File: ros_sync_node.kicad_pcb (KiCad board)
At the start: 2 copper layers, 42.5 x 38.5 mm, 16 parts, among them J1 Conn_01x03_Male, J10 5V_In, J11 3V3_Out, J2 Conn_01x03_Male, J3 Conn_01x03_Male, J4 Conn_01x03_Male, J5 Conn_01x03_Male, J6 Conn_01x03_Male, J7 Conn_01x03_Male, J8 Conn_01x03_Male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

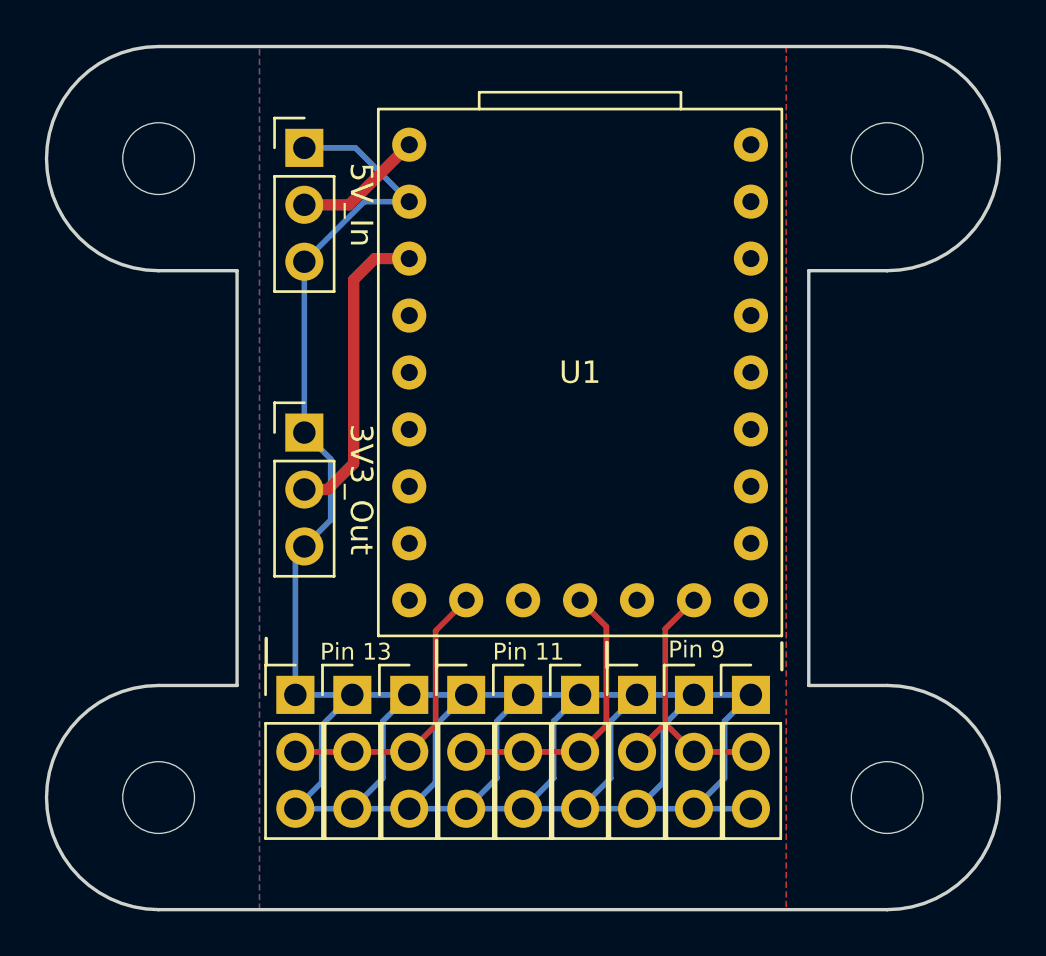
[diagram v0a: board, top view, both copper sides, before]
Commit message: Added mousebites and a readme
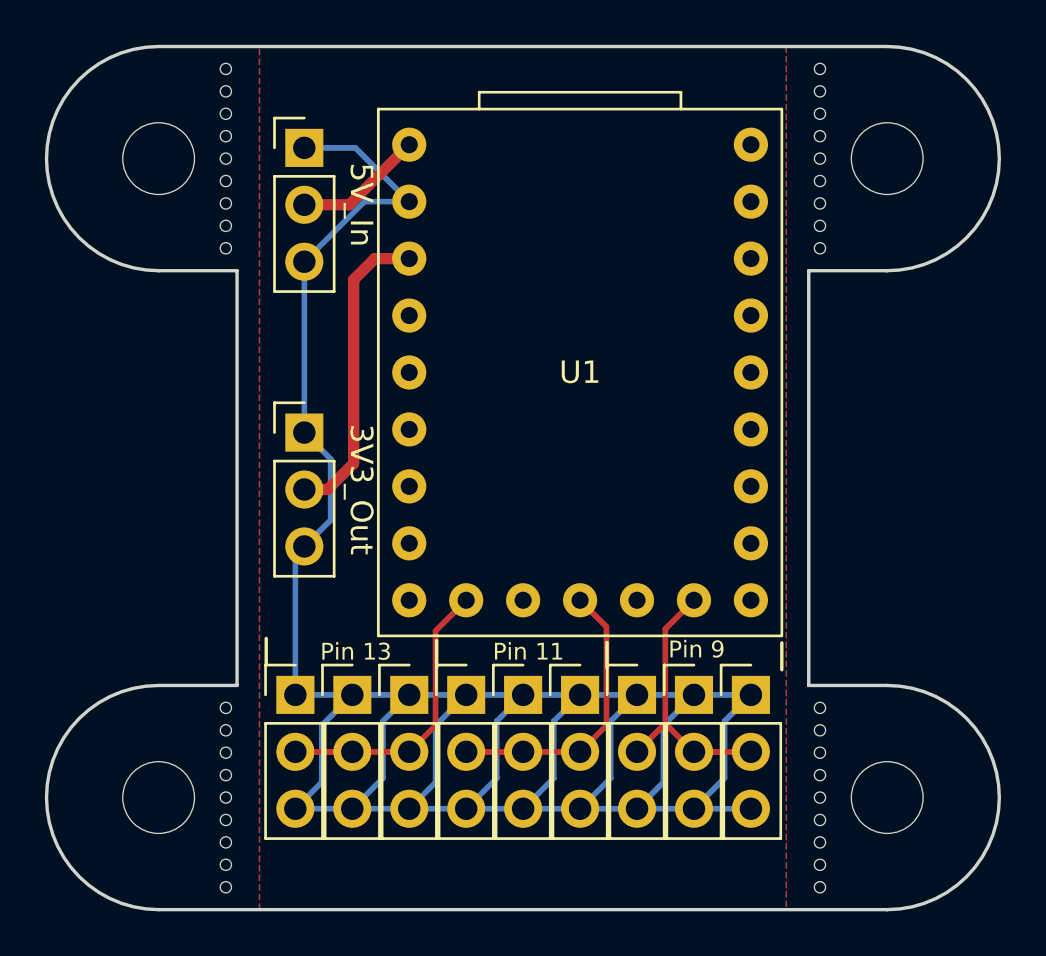
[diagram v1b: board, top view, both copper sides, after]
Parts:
- added H10: MountingHole, other:OSHTab, F.Cu at (176.0, 99.5)
- added H11: MountingHole, other:OSHTab, F.Cu at (176.0, 68.0)
- added H12: MountingHole, other:OSHTab, F.Cu at (176.0, 102.5)
- added H13: MountingHole, other:OSHTab, F.Cu at (176.0, 71.0)
- added H14: MountingHole, other:OSHTab, F.Cu at (149.5, 102.5)
- added H15: MountingHole, other:OSHTab, F.Cu at (149.5, 99.5)
- added H16: MountingHole, other:OSHTab, F.Cu at (176.0, 74.0)
- added H5: MountingHole, other:OSHTab, F.Cu at (149.5, 74.0)
- added H6: MountingHole, other:OSHTab, F.Cu at (149.5, 96.5)
- added H7: MountingHole, other:OSHTab, F.Cu at (149.5, 71.0)
- added H8: MountingHole, other:OSHTab, F.Cu at (149.5, 68.0)
- added H9: MountingHole, other:OSHTab, F.Cu at (176.0, 96.5)
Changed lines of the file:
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@@
     (tracks 57)
     (zones 0)
-    (modules 16)
+    (modules 28)
     (nets 24)
   )
@@
     (add_net +5V)
   )
+  (module other:OSHTab (layer F.Cu)
+    (at 176 74 270)
+    (descr "0.5mm holes and 3mm wide tab")
+    (tags "OSHPark recommended panel tab")
+    (attr virtual)
+    (fp_text reference H16 (at 0 -1.25 90) (layer F.Fab) hide
+      (effects (font (size 1 1) (thickness 0.15)))
+    )
+    (fp_text value MountingHole (at 0 1.25 90) (layer F.Fab)
+      (effects (font (size 1 1) (thickness 0.15)))
+    )
+    (pad "" np_thru_hole circle (at 1 0 270) (size 0.5 0.5) (drill 0.5) (layers *.Cu))
+    (pad "" np_thru_hole circle (at -1 0 270) (size 0.5 0.5) (drill 0.5) (layers *.Cu))
+    (pad "" np_thru_hole circle (at 0 0 270) (size 0.5 0.5) (drill 0.5) (layers *.Cu))
+  )
+  (module other:OSHTab (layer F.Cu)
+    (at 149.5 99.5 90)
+    (descr "0.5mm holes and 3mm wide tab")
+    (tags "OSHPark recommended panel tab")
+    (attr virtual)
+    (fp_text reference H15 (at 0 -1.25 90) (layer F.Fab) hide
+      (effects (font (size 1 1) (thickness 0.15)))
+    )
+    (fp_text value MountingHole (at 0 1.25 90) (layer F.Fab)
+      (effects (font (size 1 1) (thickness 0.15)))
+    )
+    (pad "" np_thru_hole circle (at 1 0 90) (size 0.5 0.5) (drill 0.5) (layers *.Cu))
+    (pad "" np_thru_hole circle (at -1 0 90) (size 0.5 0.5) (drill 0.5) (layers *.Cu))
+    (pad "" np_thru_hole circle (at 0 0 90) (size 0.5 0.5) (drill 0.5) (layers *.Cu))
+  )
+  (module other:OSHTab (layer F.Cu)
+    (at 149.5 102.5 90)
+    (descr "0.5mm holes and 3mm wide tab")
+    (tags "OSHPark recommended panel tab")
+    (attr virtual)
+    (fp_text reference H14 (at 0 -1.25 90) (layer F.Fab) hide
+      (effects (font (size 1 1) (thickness 0.15)))
+    )
+    (fp_text value MountingHole (at 0 1.25 90) (layer F.Fab)
+      (effects (font (size 1 1) (thickness 0.15)))
+    )
+    (pad "" np_thru_hole circle (at 1 0 90) (size 0.5 0.5) (drill 0.5) (layers *.Cu))
+    (pad "" np_thru_hole circle (at -1 0 90) (size 0.5 0.5) (drill 0.5) (layers *.Cu))
+    (pad "" np_thru_hole circle (at 0 0 90) (size 0.5 0.5) (drill 0.5) (layers *.Cu))
+  )
+  (module other:OSHTab (layer F.Cu)
+    (at 176 71 270)
+    (descr "0.5mm holes and 3mm wide tab")
+    (tags "OSHPark recommended panel tab")
+    (attr virtual)
+    (fp_text reference H13 (at 0 -1.25 90) (layer F.Fab) hide
+      (effects (font (size 1 1) (thickness 0.15)))
+    )
+    (fp_text value MountingHole (at 0 1.25 90) (layer F.Fab)
+      (effects (font (size 1 1) (thickness 0.15)))
+    )
+    (pad "" np_thru_hole circle (at 1 0 270) (size 0.5 0.5) (drill 0.5) (layers *.Cu))
+    (pad "" np_thru_hole circle (at -1 0 270) (size 0.5 0.5) (drill 0.5) (layers *.Cu))
+    (pad "" np_thru_hole circle (at 0 0 270) (size 0.5 0.5) (drill 0.5) (layers *.Cu))
+  )
+  (module other:OSHTab (layer F.Cu)
+    (at 176 102.5 270)
+    (descr "0.5mm holes and 3mm wide tab")
+    (tags "OSHPark recommended panel tab")
+    (attr virtual)
+    (fp_text reference H12 (at 0 -1.25 90) (layer F.Fab) hide
+      (effects (font (size 1 1) (thickness 0.15)))
+    )
+    (fp_text value MountingHole (at 0 1.25 90) (layer F.Fab)
+      (effects (font (size 1 1) (thickness 0.15)))
+    )
+    (pad "" np_thru_hole circle (at 1 0 270) (size 0.5 0.5) (drill 0.5) (layers *.Cu))
+    (pad "" np_thru_hole circle (at -1 0 270) (size 0.5 0.5) (drill 0.5) (layers *.Cu))
+    (pad "" np_thru_hole circle (at 0 0 270) (size 0.5 0.5) (drill 0.5) (layers *.Cu))
+  )
+  (module other:OSHTab (layer F.Cu)
+    (at 176 68 270)
+    (descr "0.5mm holes and 3mm wide tab")
+    (tags "OSHPark recommended panel tab")
+    (attr virtual)
+    (fp_text reference H11 (at 0 -1.25 90) (layer F.Fab) hide
+      (effects (font (size 1 1) (thickness 0.15)))
+    )
+    (fp_text value MountingHole (at 0 1.25 90) (layer F.Fab)
+      (effects (font (size 1 1) (thickness 0.15)))
+    )
+    (pad "" np_thru_hole circle (at 1 0 270) (size 0.5 0.5) (drill 0.5) (layers *.Cu))
+    (pad "" np_thru_hole circle (at -1 0 270) (size 0.5 0.5) (drill 0.5) (layers *.Cu))
+    (pad "" np_thru_hole circle (at 0 0 270) (size 0.5 0.5) (drill 0.5) (layers *.Cu))
+  )
+  (module other:OSHTab (layer F.Cu)
+    (at 176 99.5 270)
+    (descr "0.5mm holes and 3mm wide tab")
+    (tags "OSHPark recommended panel tab")
+    (attr virtual)
+    (fp_text reference H10 (at 0 -1.25 90) (layer F.Fab) hide
+      (effects (font (size 1 1) (thickness 0.15)))
+    )
+    (fp_text value MountingHole (at 0 1.25 90) (layer F.Fab)
+      (effects (font (size 1 1) (thickness 0.15)))
+    )
+    (pad "" np_thru_hole circle (at 1 0 270) (size 0.5 0.5) (drill 0.5) (layers *.Cu))
+    (pad "" np_thru_hole circle (at -1 0 270) (size 0.5 0.5) (drill 0.5) (layers *.Cu))
+    (pad "" np_thru_hole circle (at 0 0 270) (size 0.5 0.5) (drill 0.5) (layers *.Cu))
+  )
+  (module other:OSHTab (layer F.Cu)
+    (at 176 96.5 270)
+    (descr "0.5mm holes and 3mm wide tab")
+    (tags "OSHPark recommended panel tab")
+    (attr virtual)
+    (fp_text reference H9 (at 0 -1.25 90) (layer F.Fab) hide
+      (effects (font (size 1 1) (thickness 0.15)))
+    )
+    (fp_text value MountingHole (at 0 1.25 90) (layer F.Fab)
+      (effects (font (size 1 1) (thickness 0.15)))
+    )
+    (pad "" np_thru_hole circle (at 1 0 270) (size 0.5 0.5) (drill 0.5) (layers *.Cu))
+    (pad "" np_thru_hole circle (at -1 0 270) (size 0.5 0.5) (drill 0.5) (layers *.Cu))
+    (pad "" np_thru_hole circle (at 0 0 270) (size 0.5 0.5) (drill 0.5) (layers *.Cu))
+  )
+  (module other:OSHTab (layer F.Cu)
+    (at 149.5 68 90)
+    (descr "0.5mm holes and 3mm wide tab")
+    (tags "OSHPark recommended panel tab")
+    (attr virtual)
+    (fp_text reference H8 (at 0 -1.25 90) (layer F.Fab) hide
+      (effects (font (size 1 1) (thickness 0.15)))
+    )
+    (fp_text value MountingHole (at 0 1.25 90) (layer F.Fab)
+      (effects (font (size 1 1) (thickness 0.15)))
+    )
+    (pad "" np_thru_hole circle (at 1 0 90) (size 0.5 0.5) (drill 0.5) (layers *.Cu))
+    (pad "" np_thru_hole circle (at -1 0 90) (size 0.5 0.5) (drill 0.5) (layers *.Cu))
+    (pad "" np_thru_hole circle (at 0 0 90) (size 0.5 0.5) (drill 0.5) (layers *.Cu))
+  )
+  (module other:OSHTab (layer F.Cu)
+    (at 149.5 71 90)
+    (descr "0.5mm holes and 3mm wide tab")
+    (tags "OSHPark recommended panel tab")
+    (attr virtual)
+    (fp_text reference H7 (at 0 -1.25 90) (layer F.Fab) hide
+      (effects (font (size 1 1) (thickness 0.15)))
+    )
+    (fp_text value MountingHole (at 0 1.25 90) (layer F.Fab)
+      (effects (font (size 1 1) (thickness 0.15)))
+    )
+    (pad "" np_thru_hole circle (at 1 0 90) (size 0.5 0.5) (drill 0.5) (layers *.Cu))
+    (pad "" np_thru_hole circle (at -1 0 90) (size 0.5 0.5) (drill 0.5) (layers *.Cu))
+    (pad "" np_thru_hole circle (at 0 0 90) (size 0.5 0.5) (drill 0.5) (layers *.Cu))
+  )
+  (module other:OSHTab (layer F.Cu)
+    (at 149.5 96.5 90)
+    (descr "0.5mm holes and 3mm wide tab")
+    (tags "OSHPark recommended panel tab")
+    (attr virtual)
+    (fp_text reference H6 (at 0 -1.25 90) (layer F.Fab) hide
+      (effects (font (size 1 1) (thickness 0.15)))
+    )
+    (fp_text value MountingHole (at 0 1.25 90) (layer F.Fab)
+      (effects (font (size 1 1) (thickness 0.15)))
+    )
+    (pad "" np_thru_hole circle (at 1 0 90) (size 0.5 0.5) (drill 0.5) (layers *.Cu))
+    (pad "" np_thru_hole circle (at -1 0 90) (size 0.5 0.5) (drill 0.5) (layers *.Cu))
+    (pad "" np_thru_hole circle (at 0 0 90) (size 0.5 0.5) (drill 0.5) (layers *.Cu))
+  )
+  (module other:OSHTab (layer F.Cu)
+    (at 149.5 74 90)
+    (descr "0.5mm holes and 3mm wide tab")
+    (tags "OSHPark recommended panel tab")
+    (attr virtual)
+    (fp_text reference H5 (at 0 -1.25 90) (layer F.Fab) hide
+      (effects (font (size 1 1) (thickness 0.15)))
+    )
+    (fp_text value MountingHole (at 0 1.25 90) (layer F.Fab)
+      (effects (font (size 1 1) (thickness 0.15)))
+    )
+    (pad "" np_thru_hole circle (at 1 0 90) (size 0.5 0.5) (drill 0.5) (layers *.Cu))
+    (pad "" np_thru_hole circle (at -1 0 90) (size 0.5 0.5) (drill 0.5) (layers *.Cu))
+    (pad "" np_thru_hole circle (at 0 0 90) (size 0.5 0.5) (drill 0.5) (layers *.Cu))
+  )
   (module MountingHole:MountingHole_3.2mm_M3 (layer F.Cu)

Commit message: Added output pin for the neopixels.  Update to KiCAD 7
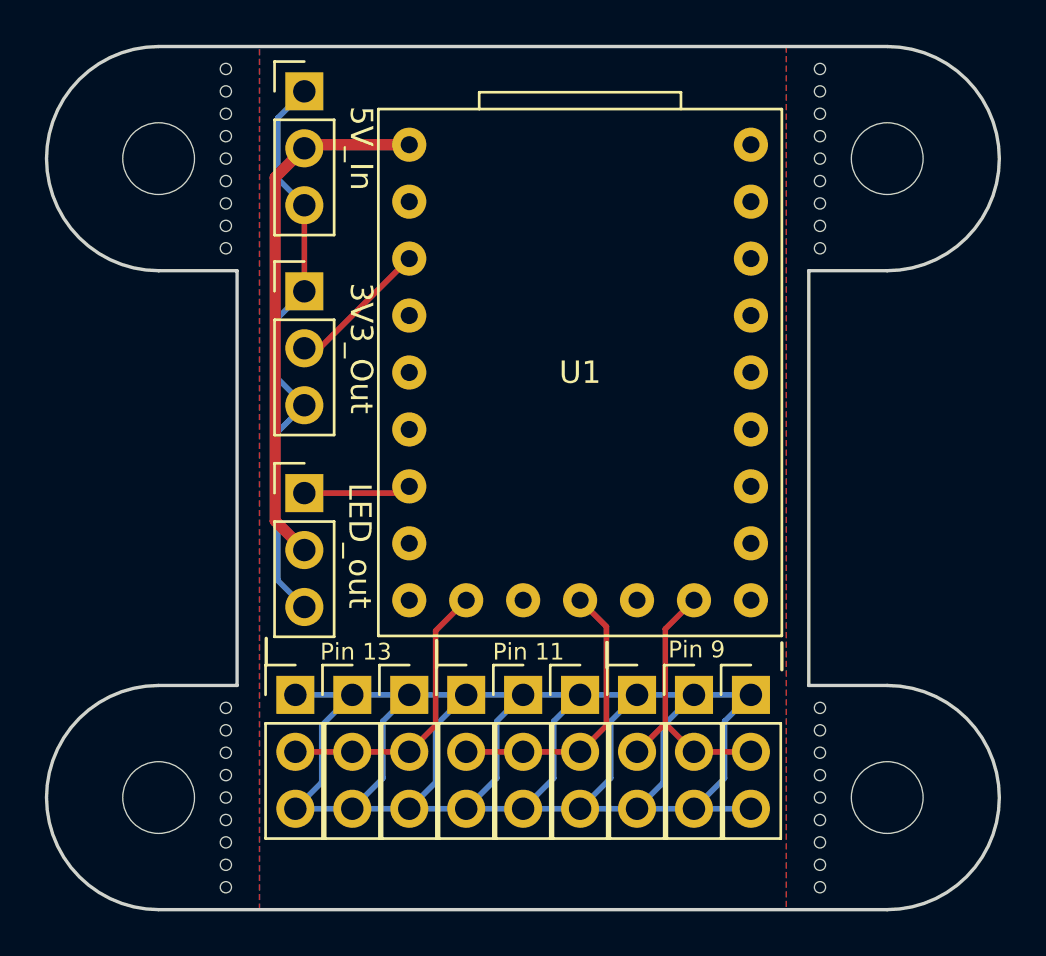
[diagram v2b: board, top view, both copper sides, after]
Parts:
- added J12: LED_out, Connector_PinHeader_2.54mm:PinHeader_1x03_P2.54mm_Vertical, F.Cu at (153.0, 85.9)
- J1, J2, J3, J4, J5, J6, J7, J8, J9: value Conn_01x03_Male -> Conn_01x03_Pin
- moved J11 6.30 mm to (153.0, 76.9)
- moved J10 2.52 mm to (153.0, 68.0)
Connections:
- net +3V3 renamed +3.3V
- U1 pad 0: Net-(U1-Pad0) -> unconnected-(U1-Pad0)
- U1 pad 1: Net-(U1-Pad1) -> unconnected-(U1-Pad1)
- U1 pad 10: Net-(U1-Pad10) -> unconnected-(U1-Pad10)
- U1 pad 12: Net-(U1-Pad12) -> unconnected-(U1-Pad12)
- U1 pad 14: Net-(U1-Pad14) -> unconnected-(U1-Pad14)
- U1 pad 15: Net-(U1-Pad15) -> unconnected-(U1-Pad15)
- U1 pad 2: Net-(U1-Pad2) -> unconnected-(U1-Pad2)
- U1 pad 27: Net-(U1-Pad27) -> unconnected-(U1-Pad27)
- U1 pad 28: Net-(U1-Pad28) -> unconnected-(U1-Pad28)
- U1 pad 29: Net-(U1-Pad29) -> unconnected-(U1-Pad29)
- U1 pad 3: Net-(U1-Pad3) -> unconnected-(U1-Pad3)
- U1 pad 4: Net-(U1-Pad4) -> unconnected-(U1-Pad4)
- U1 pad 5: Net-(U1-Pad5) -> unconnected-(U1-Pad5)
- U1 pad 6: Net-(U1-Pad6) -> unconnected-(U1-Pad6)
- U1 pad 7: Net-(U1-Pad7) -> unconnected-(U1-Pad7)
- U1 pad 8: Net-(U1-Pad8) -> unconnected-(U1-Pad8)
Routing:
- net +5V: track 6.19 -> 23.7 mm
- net +3.3V: track 14.1 -> 6.34 mm
- net Earth: track 121.6 -> 115.6 mm
- net Net-(J12-Pin_1): track 0.00 -> 4.80 mm
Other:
- net class Default removed
- net class Power removed
- board text added: "Sync Node v1.1 MA - 2023"
- board text removed: "Sync Node v1 MA - 2022"

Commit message: Fixed some text
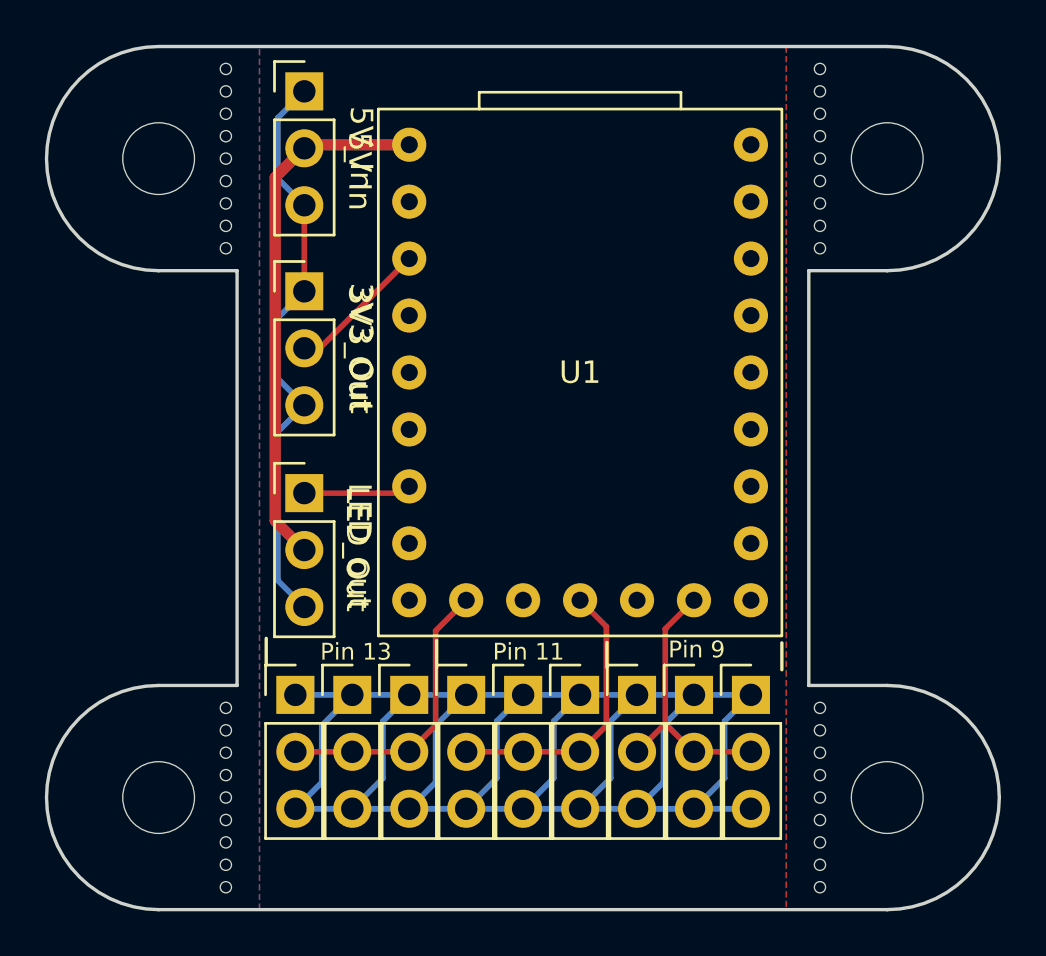
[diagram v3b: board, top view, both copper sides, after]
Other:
- board text added: "3V3 Out"
- board text added: "5V In"
- board text added: "LED Out"
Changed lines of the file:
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@@
         (effects (font (size 1 1) (thickness 0.15)))
     )
-    (fp_text value "LED_out" (at 2.46662 2.345009 -90 unlocked) (layer "F.SilkS")
+    (fp_text value "LED_out" (at 2.46662 2.345009 270 unlocked) (layer "F.SilkS")
         (effects (font (size 1 1) (thickness 0.15)))
     )
@@
     (effects (font (size 0.75 0.75) (thickness 0.1)))
   )
+  (gr_text "5V In" (at 155.469556 71.567633 270) (layer "F.SilkS")
+    (effects (font (size 1 1) (thickness 0.15)))
+  )
+  (gr_text "LED Out" (at 155.363581 88.417702 -90) (layer "F.SilkS")
+    (effects (font (size 1 1) (thickness 0.15)))
+  )
+  (gr_text "3V3 Out" (at 155.469556 79.462791 270) (layer "F.SilkS")
+    (effects (font (size 1 1) (thickness 0.15)))
+  )
   (gr_text "Pin 13" (at 155.3 93) (layer "F.SilkS")
